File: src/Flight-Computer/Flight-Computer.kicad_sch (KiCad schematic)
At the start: 4 parts, among them U1 STM32H750VBTx

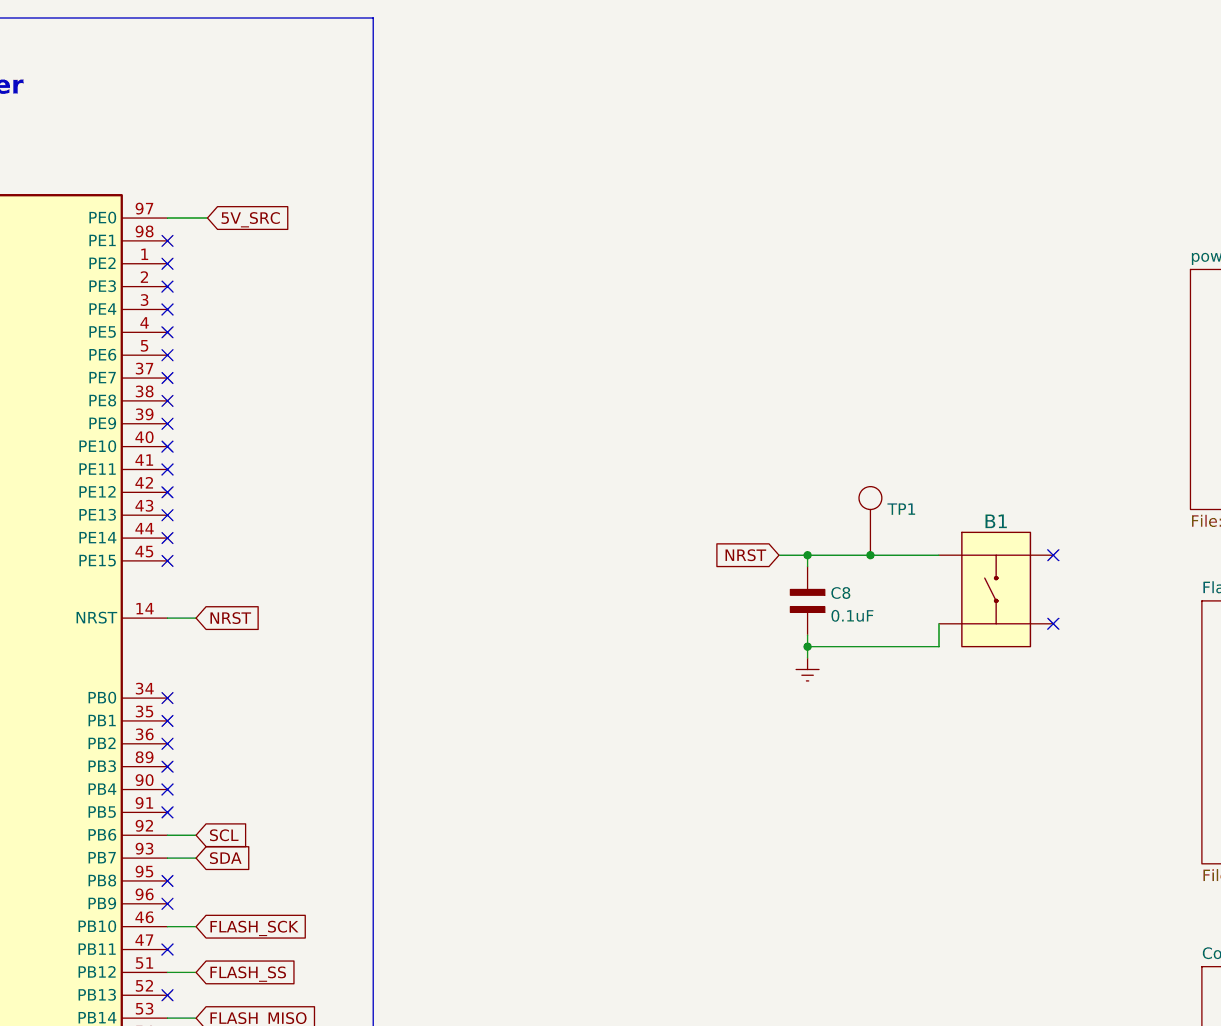
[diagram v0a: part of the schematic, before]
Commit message: implemented rgb led in schematic
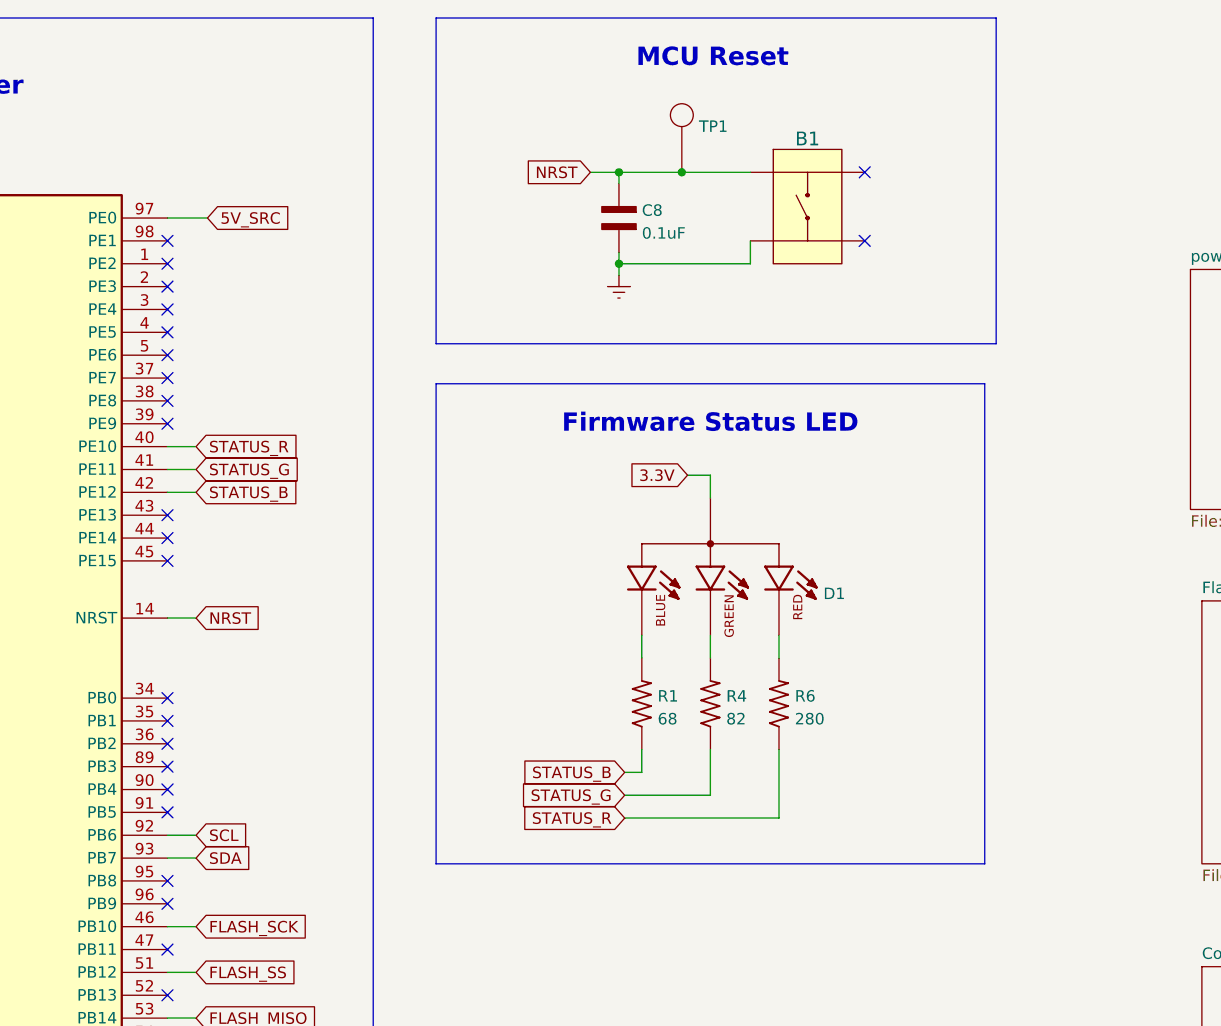
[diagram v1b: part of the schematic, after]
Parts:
- added D1: CLMVC-FKA-CL1D1L71BB7C3C3, LED_CLMVC-FKA-CL1D1L71BB7C3C3, symbol Flight-Computer:CLMVC-FKA-CL1D1L71BB7C3C3
- added R1: 68, symbol Flight-Computer:RES_0603
- added R4: 82, symbol Flight-Computer:RES_0603
- added R6: 280, symbol Flight-Computer:RES_0603
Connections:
- net 3.3V: now also D1.1
- net STATUS_R: now reaches U1.40 (PE10)
- net STATUS_R: now also R6.1
- net STATUS_G: now reaches U1.41 (PE11)
- net STATUS_G: now also R4.1
- net STATUS_B: now reaches U1.42 (PE12)
- net STATUS_B: now also R1.1
- new net: D1.3, R4.2
- new net: D1.2, R1.2
- new net: D1.4, R6.2
- no-connect marks 72 -> 69
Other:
- note added: "Firmware Status LED"
- note added: "MCU Reset"
- moved on the sheet: B1, C8, TP1

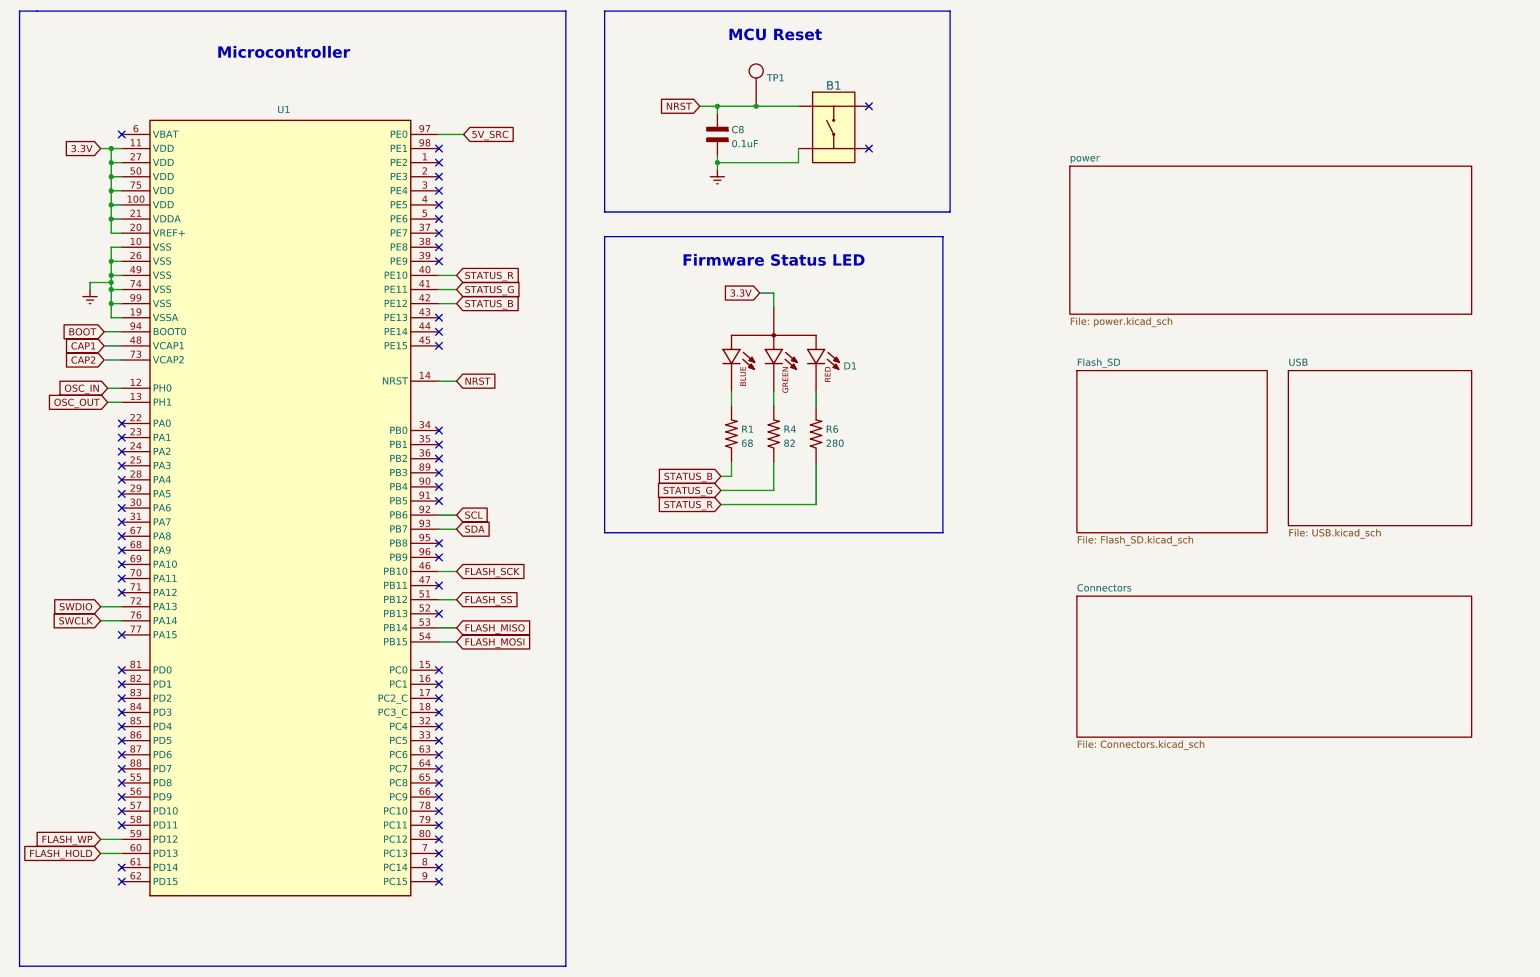
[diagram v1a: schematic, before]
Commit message: added logo and mounting holes to schematic
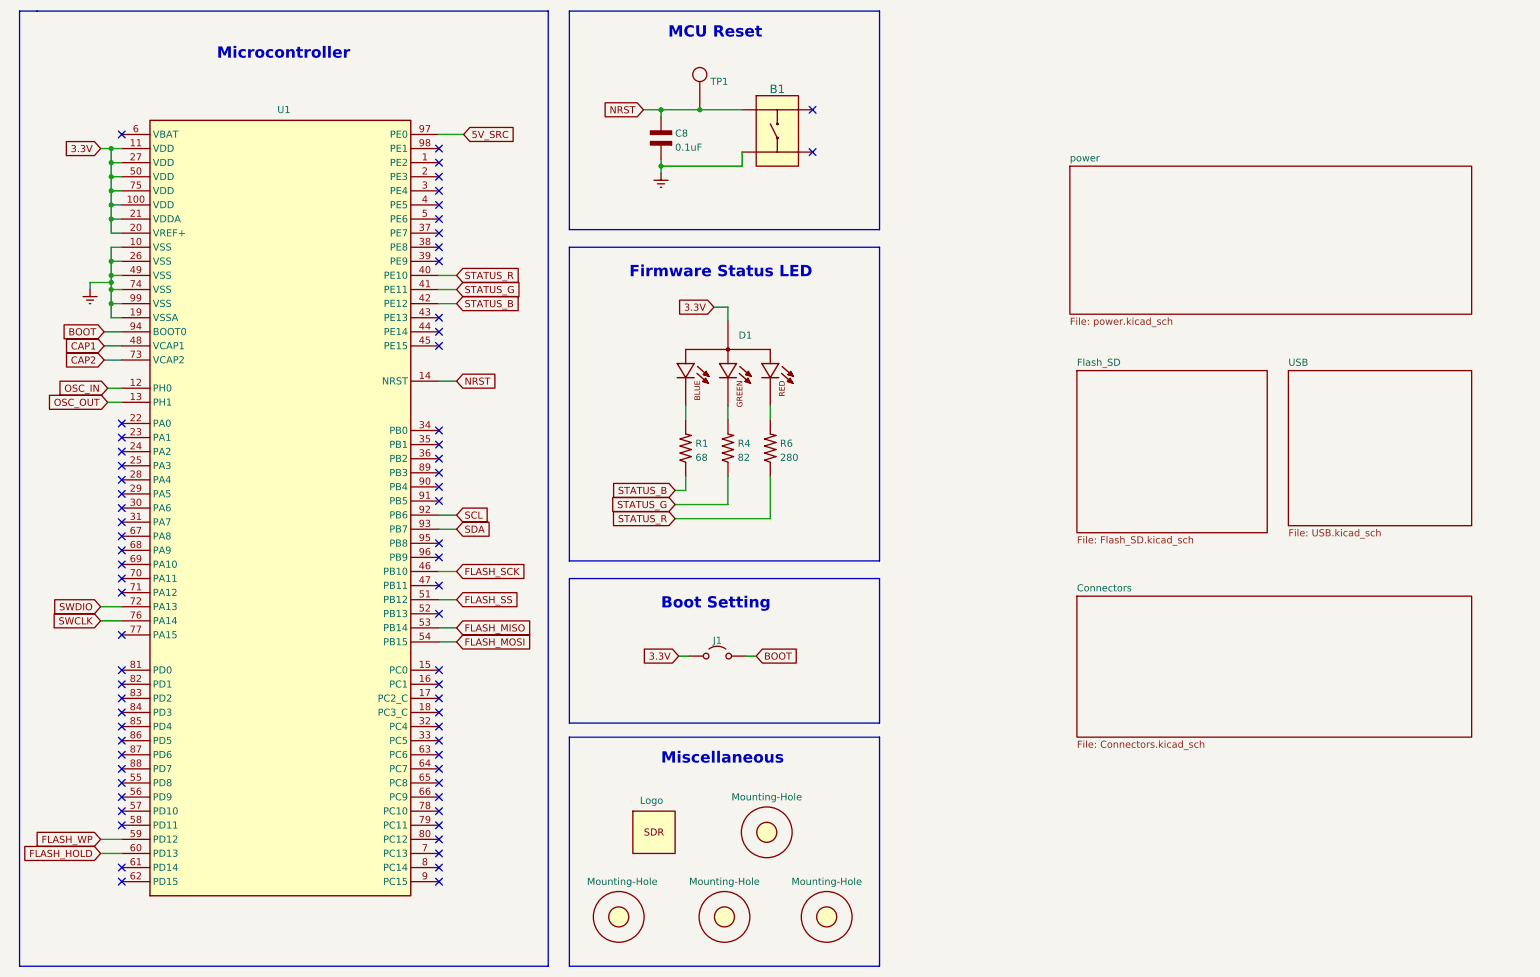
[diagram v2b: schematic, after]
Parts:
- added H1, H2, H3, H4: Mounting-Hole, symbol Flight-Computer:Mounting-Hole
- added J1: Jumper_NO, symbol Flight-Computer:Jumper_NO
- added LOGO1: Logo, symbol Flight-Computer:Logo
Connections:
- net 3.3V: now also J1.1 (A)
- net BOOT: now also J1.2 (B)
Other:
- note added: "Boot Setting"
- note added: "Miscellaneous"
- moved on the sheet: B1, C8, D1, R1, R4, R6, TP1

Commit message: implemented crystal oscillator in schematic
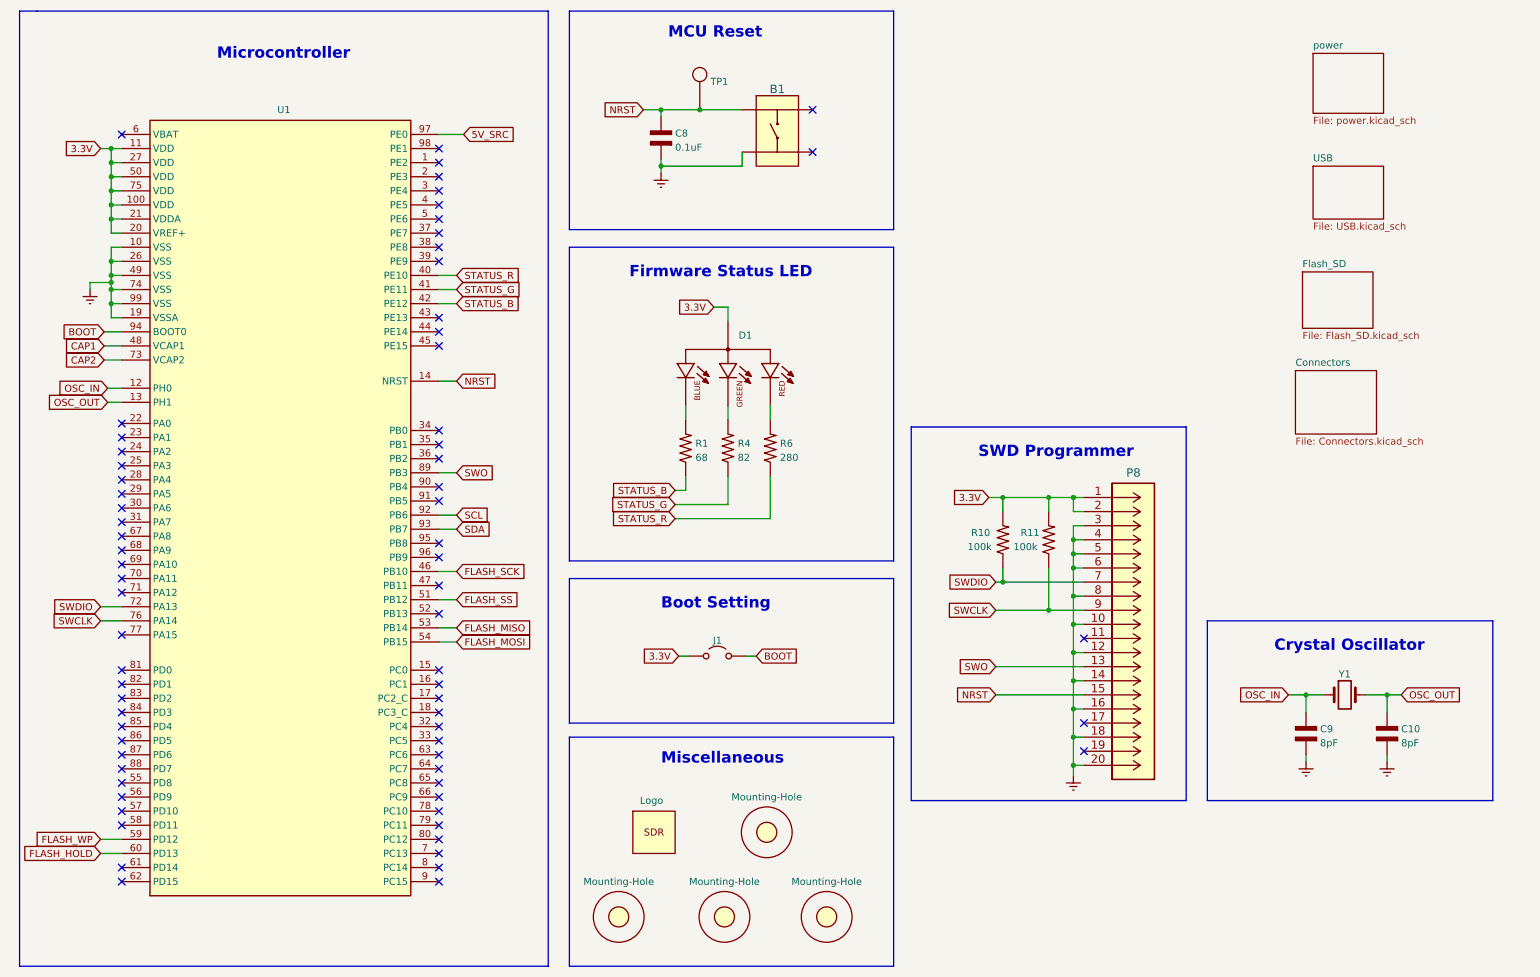
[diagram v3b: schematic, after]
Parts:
- added C10, C9: 8pF, symbol Flight-Computer:CAP_0603
- added P8: 3220-20-0200-00, CONN20_D10-RA-BK_SUL, symbol Flight-Computer:3220-20-0200-00
- added R10, R11: 100k, symbol Flight-Computer:RES_0603
- added Y1: ECS-240-18-33-JGN-TR, symbol Flight-Computer:ECS-240-18-33-JGN-TR
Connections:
- net 3.3V: now also P8.1, P8.2, R10.2, R11.2
- net Earth: now also C10.2, C9.2, P8.10, P8.12, P8.14, P8.16, P8.18, P8.20, P8.3, P8.4, P8.5, P8.6, P8.8
- net NRST: now also P8.15
- net OSC_IN: now also C9.1, Y1.1
- net OSC_OUT: now also C10.1, Y1.3
- net SWCLK: now also P8.9, R11.1
- net SWDIO: now also P8.7, R10.1
- net SWO: now reaches U1.89 (PB3)
- net SWO: now also P8.13
- no-connect marks 69 -> 71
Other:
- note added: "Crystal Oscillator"
- note added: "SWD Programmer"

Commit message: implemented mcu decoupling and regulator caps in schematic
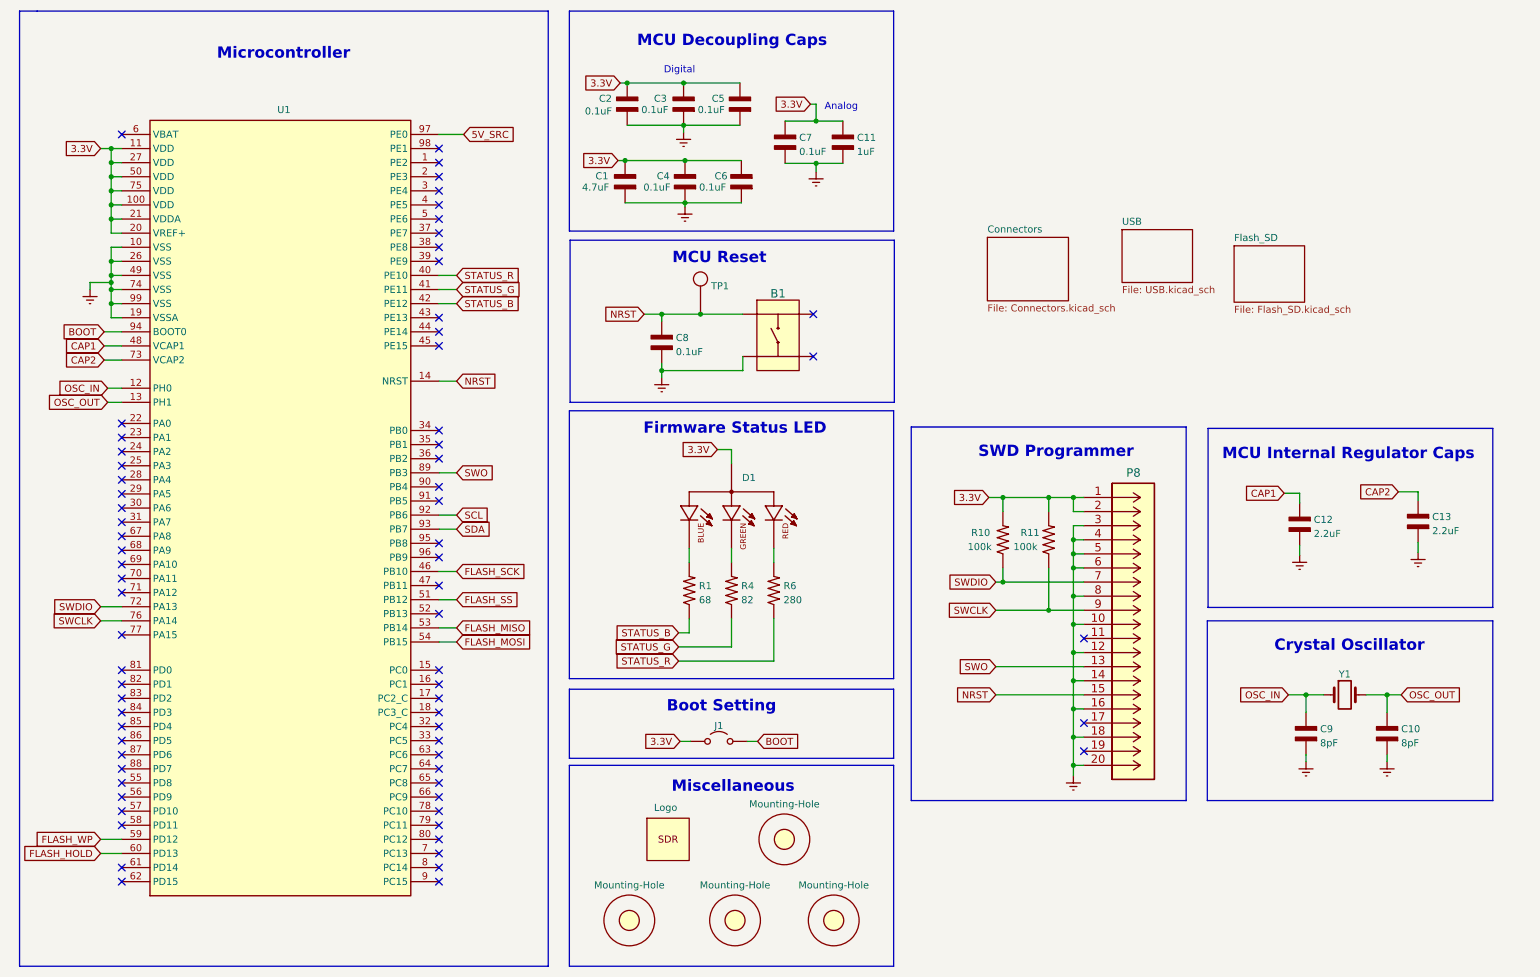
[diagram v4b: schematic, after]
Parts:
- added C1: 4.7uF, symbol Flight-Computer:CAP_0603
- added C11: 1uF, symbol Flight-Computer:CAP_0603
- added C12, C13: 2.2uF, symbol Flight-Computer:CAP_0603
- added C2, C3, C4, C5, C6, C7: 0.1uF, symbol Flight-Computer:CAP_0603
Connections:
- net 3.3V: now also C1.1, C11.1, C2.1, C3.1, C4.1, C5.1, C6.1, C7.1
- net CAP1: now also C12.1
- net CAP2: now also C13.1
- net Earth: now also C1.2, C11.2, C12.2, C13.2, C2.2, C3.2, C4.2, C5.2, C6.2, C7.2
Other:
- removed sheet power
- note added: "Analog"
- note added: "Digital"
- note added: "MCU Decoupling Caps"
- note added: "MCU Internal Regulator Caps"
- moved on the sheet: B1, C8, D1, J1, R1, R4, R6, TP1
